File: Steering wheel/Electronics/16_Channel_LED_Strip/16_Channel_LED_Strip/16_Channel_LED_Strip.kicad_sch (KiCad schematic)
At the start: 35 parts, among them IC1 TLC59116FIPWR, J1 INPUT

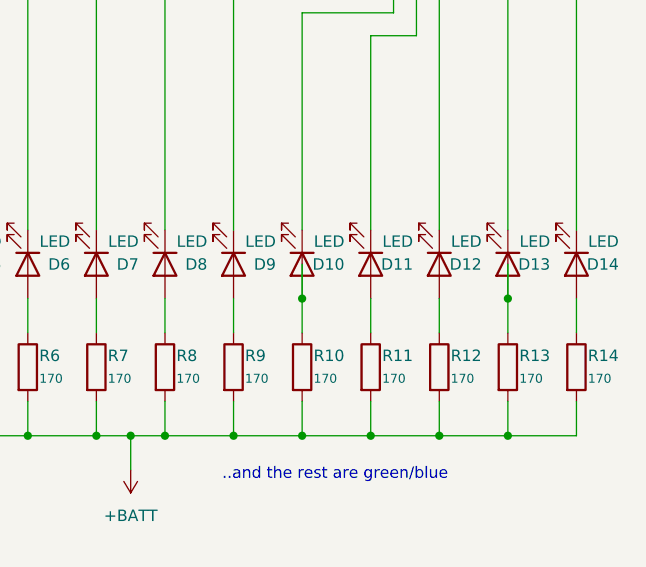
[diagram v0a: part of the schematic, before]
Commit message: Finish LED PCB [Ordered]
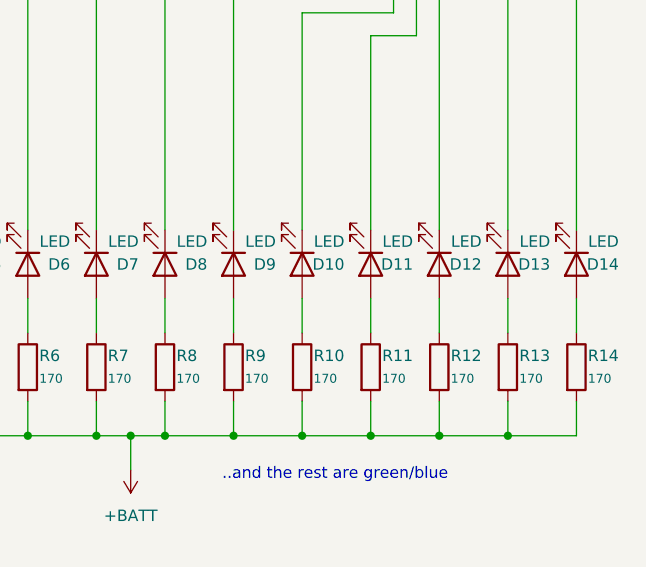
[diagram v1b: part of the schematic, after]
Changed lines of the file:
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@@
   (junction (at 186.69 149.86) (diameter 0) (color 0 0 0 0)
   )
-  (junction (at 171.45 134.62) (diameter 0) (color 0 0 0 0)
-  )
   (junction (at 175.26 52.07) (diameter 0) (color 0 0 0 0)
   )
   (junction (at 171.45 52.07) (diameter 0) (color 0 0 0 0)
   )
-  (junction (at 194.31 134.62) (diameter 0) (color 0 0 0 0)
-  )
   (junction (at 156.21 149.86) (diameter 0) (color 0 0 0 0)
   )
@@
     (stroke (width 0) (type default))
   )
-  (wire (pts (xy 171.45 130.81) (xy 171.45 134.62))
-    (stroke (width 0) (type default))
-  )
   (wire (pts (xy 102.87 146.05) (xy 102.87 149.86))
     (stroke (width 0) (type default))
@@
     (stroke (width 0) (type default))
   )
-  (wire (pts (xy 194.31 130.81) (xy 194.31 134.62))
-    (stroke (width 0) (type default))
-  )
